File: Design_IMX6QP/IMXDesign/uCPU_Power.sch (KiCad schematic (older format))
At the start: 59 parts, among them U1 MCIMX6QP5EVT

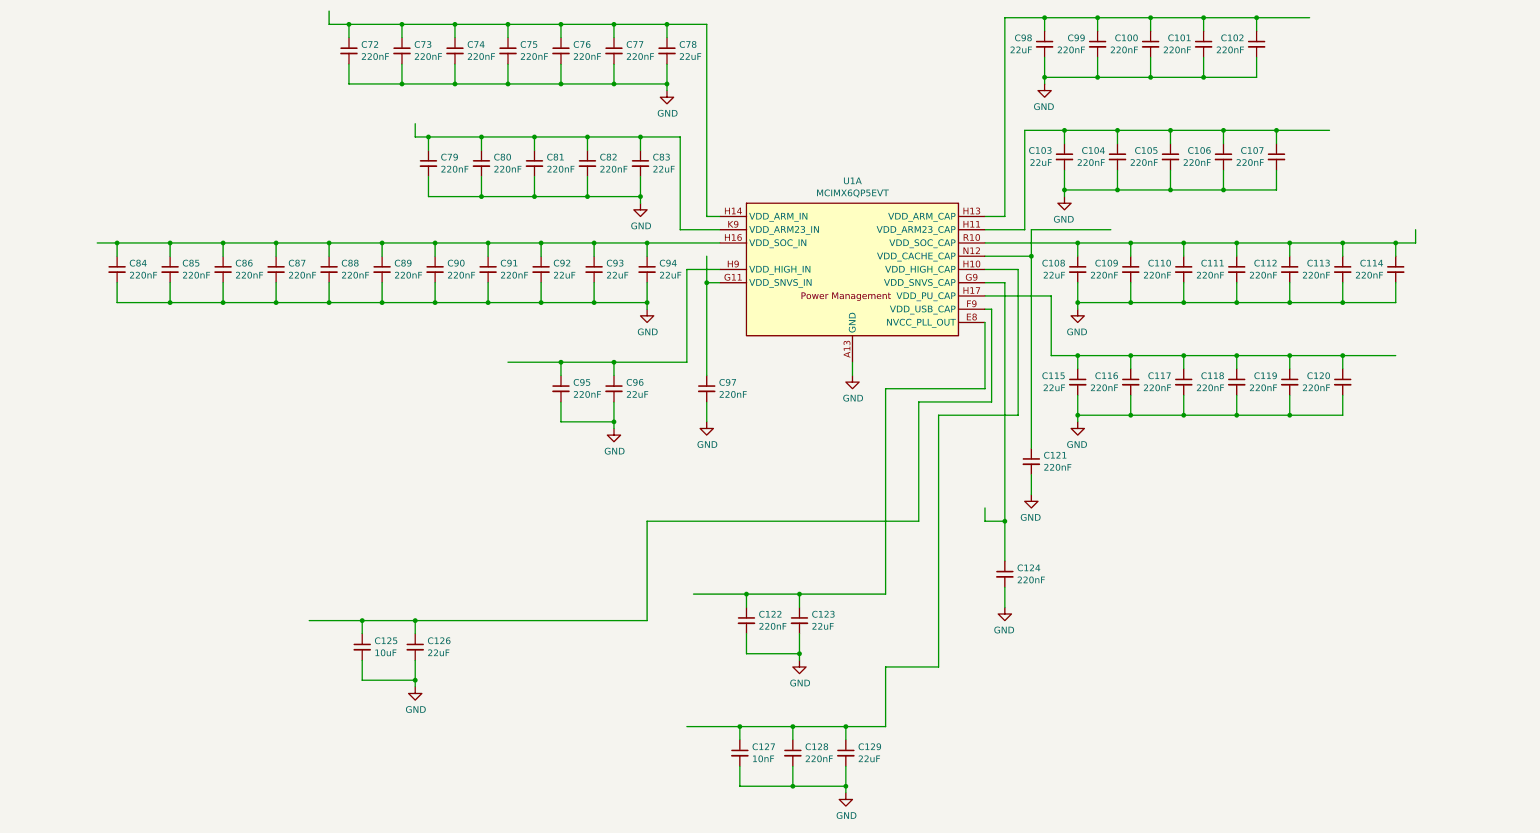
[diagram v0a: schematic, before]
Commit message: Update IMX6QP and IMX8MQ
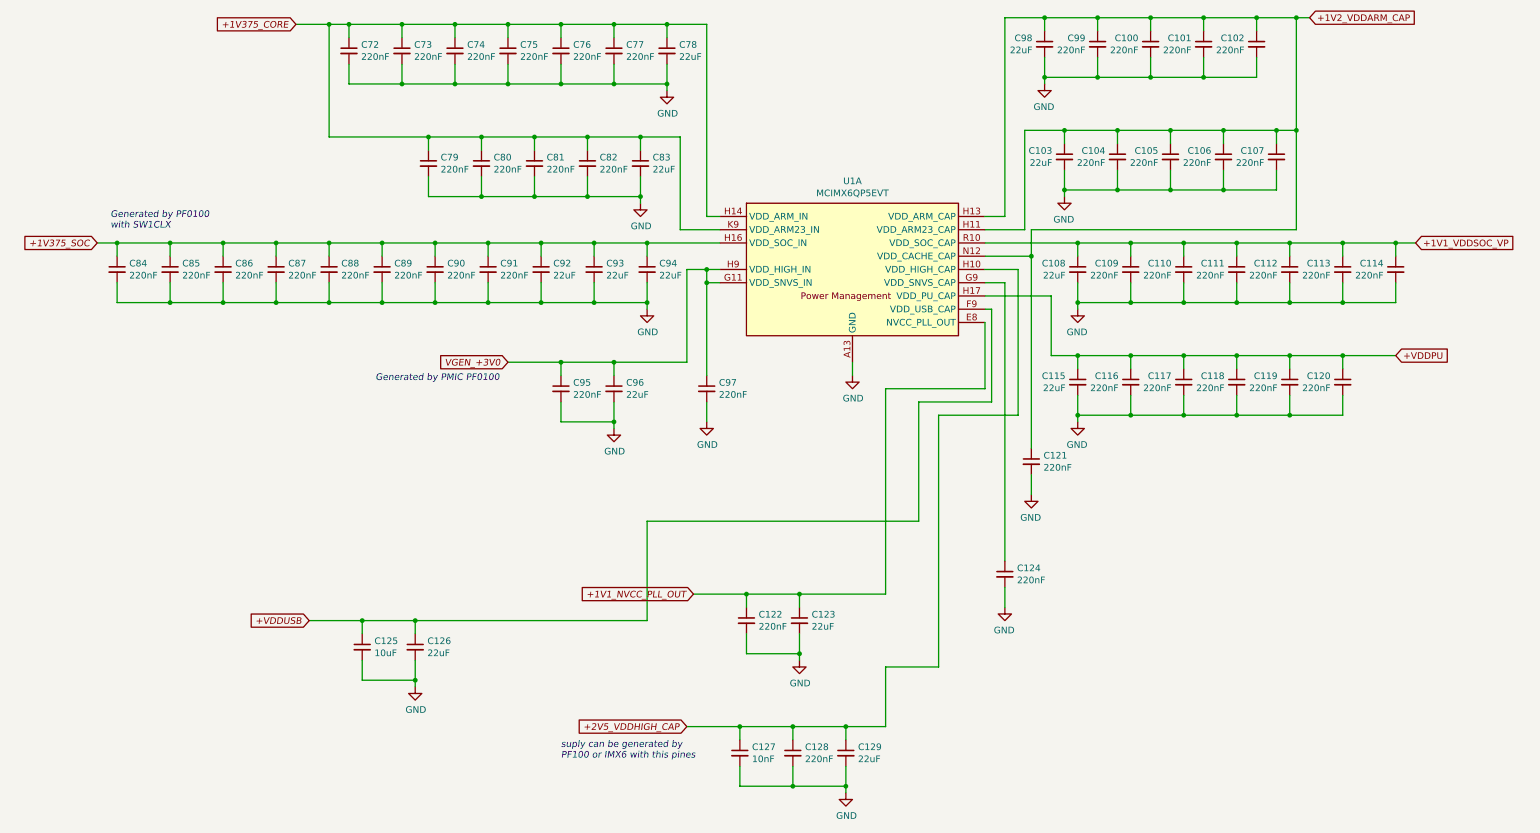
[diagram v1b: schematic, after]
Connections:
- net labels added: +1V1_NVCC_PLL_OUT, +1V1_VDDSOC_VP, +1V2_VDDARM_CAP, +1V375_CORE, +1V375_SOC, +2V5_VDDHIGH_CAP, +VDDPU, +VDDUSB, VGEN_+3V0
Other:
- note added: "Generated by PF0100\nwith SW1CLX\n"
- note added: "Generated by PMIC PF0100"
- note added: "suply can be generated by \nPF100 or IMX6 with this pines"
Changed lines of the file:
@@
 $Descr A4 11693 8268
 encoding utf-8
-Sheet 11 12
+Sheet 6 17
 Title ""
 Date ""
@@
 	2550 900  2400 900
 Wire Wire Line
-	2400 900  2400 800
-Wire Wire Line
 	2950 1000 2950 900
 Connection ~ 2950 900
@@
 Wire Wire Line
 	5050 2450 5050 1750
-Wire Wire Line
-	3150 1750 3050 1750
-Wire Wire Line
-	3050 1750 3050 1650
 Connection ~ 3150 1750
 $Comp
@@
 $EndComp
 Wire Wire Line
-	5350 2750 5100 2750
+	5350 2750 5250 2750
 Wire Wire Line
 	5100 2750 5100 3450
@@
 Connection ~ 9400 850
 Wire Wire Line
-	9400 850  9800 850
+	9400 850  9700 850
 Wire Wire Line
 	9000 950  9000 850
@@
 Connection ~ 9550 1700
 Wire Wire Line
-	9550 1700 9950 1700
+	9550 1700 9700 1700
 Wire Wire Line
 	9150 1800 9150 1700
@@
 	10450 2550 10600 2550
 Wire Wire Line
-	10600 2550 10600 2450
-Wire Wire Line
 	10050 2650 10050 2550
 Connection ~ 10050 2550
@@
 Wire Wire Line
 	7700 2650 7700 2450
-Wire Wire Line
-	7700 2450 8300 2450
 Connection ~ 7700 2650
-Wire Wire Line
-	5250 2850 5250 2650
-Connection ~ 5250 2850
 $Comp
 L Device:C_Small C124
@@
 Wire Wire Line
 	7350 2850 7500 2850
-Wire Wire Line
-	7500 2850 7500 4650
-Wire Wire Line
-	7500 4650 7350 4650
-Wire Wire Line
-	7350 4650 7350 4550
-Connection ~ 7500 4650
-Wire Wire Line
-	7500 4650 7500 4950
 $Comp
 L Device:C_Small C123
@@
 $EndComp
 Connection ~ 3050 5400
+Text GLabel 10600 2550 2    50   Input ~ 0
++1V1_VDDSOC_VP
+Wire Wire Line
+	9700 850  9700 1700
+Connection ~ 9700 850
+Wire Wire Line
+	9700 850  9800 850
+Text GLabel 9800 850  2    50   Input ~ 0
++1V2_VDDARM_CAP
+Wire Wire Line
+	9700 2450 9700 1700
+Wire Wire Line
+	7700 2450 9700 2450
+Connection ~ 9700 1700
+Text GLabel 10450 3400 2    50   Input ~ 0
++VDDPU
+Wire Wire Line
+	7500 2850 7500 4950
+Text GLabel 5100 6200 0    50   Input Italic 0
++2V5_VDDHIGH_CAP
+Text Notes 4150 6450 0    50   Italic 0
+suply can be generated by \nPF100 or IMX6 with this pines
+Text GLabel 2250 5400 0    50   Input Italic 0
++VDDUSB
+Text GLabel 5150 5200 0    50   Input Italic 0
++1V1_NVCC_PLL_OUT
+Text GLabel 3750 3450 0    50   Input Italic 0
+VGEN_+3V0
+Wire Wire Line
+	5250 2850 5250 2750
+Connection ~ 5250 2850
+Connection ~ 5250 2750
+Wire Wire Line
+	5250 2750 5100 2750
+Text Notes 2750 3600 0    50   Italic 0
+Generated by PMIC PF0100
+Text GLabel 650  2550 0    50   Input Italic 0
++1V375_SOC
+Text Notes 750  2450 0    50   Italic 0
+Generated by PF0100\nwith SW1CLX\n
+Wire Wire Line
+	2400 1750 2400 900
+Connection ~ 2400 900
+Wire Wire Line
+	2400 1750 3150 1750
+Text GLabel 2150 900  0    50   Input Italic 0
++1V375_CORE
+Wire Wire Line
+	2150 900  2400 900
 $EndSCHEMATC
